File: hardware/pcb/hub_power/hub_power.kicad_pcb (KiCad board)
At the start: 2 copper layers, 74 x 86 mm, 58 parts, among them J1 XIAO, J10 BAT (JST-PH), J11 → 電源板, J12 → ハブ板, J13 USB-C, J2 OLED, J3 AS5600, J4 SPK IN, J5 SPK OUT, J6 REED, J7 TOGGLE, J8 BTN2, K31 G6S-2F DC5, Q1 MMUN2133LT1G, Q31 SS8050, U1 TPS61090RSAR, U2 MCP73871-2CCI/ML, U3 INA226AIDGSR

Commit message: Extended を 12 → 9 種類に減らす（$36.84 → $27.63）
🔒 2026-09-12 ユーザー「b でいいでしょ」。PowerBoost から写した定数のうち 3 つを Basic の値へ寄せた。
回路の意味はほとんど変えていない。

- R2 340kΩ（C17636・Extended）→ 330kΩ 0603 C23137（Basic）。
  LBO の閾値 0.5×(1+R1/R2) が 3.25V → 3.33V。80mV 早く知らせる側へ動く。
- R6 270kΩ（C17589・Extended）→ 220kΩ 0603 C22961、R7 100kΩ → 82kΩ 0603 C23254（どちらも Basic）。
  VPCC の分圧比 100/370=0.2703 → 82/302=0.2715 で差は 0.45%。
- C6 100µF 10V 1210（C23742・Extended・$0.45）→ 47µF 10V 1206 C96123（Basic・$0.27）を 2 個。
  Basic の 100µF は 6.3V 品しかなく、5.2V が掛かる所で耐圧を下げると残る容量が確実に減る
  （どれだけ減るかは曲線を見ていないので分からない）。耐圧 10V を保つため 2 個に分けた。
  ⚠ 足した C9 は PowerBoost に無い部品で、私が足したもの。

部品は表面実装 44 個・28 種類（Basic 19・Extended 9）。費用は約 $97 → 約 $88。

検査: check_sch 0 件・未配線 0・KiCad DRC のエラー 0（警告 99）・
      check_pcb は下限 0.15mm を割る組 0（いちばん近いのは 0.151mm）。
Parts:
- removed the R20 at (91.0, 114.0)
- removed the R5 at (90.9, 110.5)
- added LED1: RED, LED_SMD:LED_0805_2012Metric, F.Cu at (94.5, 114.0)
- added LED2: WHITE, LED_SMD:LED_0805_2012Metric, F.Cu at (94.3, 110.5)
- added Q1: MMUN2133LT1G, Package_TO_SOT_SMD:SOT-23, F.Cu at (87.0, 114.0)
- C6: value 100uF -> 47uF; footprint Capacitor_SMD:C_1210_3225Metric -> Capacitor_SMD:C_1206_3216Metric
- C9: renamed from R3; value 1.87M -> 47uF; footprint Resistor_SMD:R_0805_2012Metric -> Capacitor_SMD:C_1206_3216Metric
- R1: renamed from R2; value 340K -> 1.87M
- R13: renamed from Q1; value MMUN2133LT1G -> 200K; footprint Package_TO_SOT_SMD:SOT-23 -> Resistor_SMD:R_0805_2012Metric
- R2: renamed from R13; value 200K -> 330K
- R20: renamed from LED1; value RED -> 1K; footprint LED_SMD:LED_0805_2012Metric -> Resistor_SMD:R_0805_2012Metric
- R3: renamed from R4; value 200K -> 1.87M
- R4: renamed from R1; value 1.87M -> 200K
- R5: renamed from LED2; value WHITE -> 1K; footprint LED_SMD:LED_0805_2012Metric -> Resistor_SMD:R_0805_2012Metric
- R6: value 270K -> 220K
- R7: value 100K -> 82K
- moved R13 17.2 mm to (97.0, 100.0), turned to 90 degrees
- moved R2 14.0 mm to (87.4, 109.5), turned to 0 degrees
- moved R4 13.0 mm to (97.0, 111.0), turned to 90 degrees
- moved C9 8.38 mm to (103.1, 107.0)
- moved R3 4.52 mm to (94.9, 107.0)
- moved R20 3.50 mm to (91.0, 114.0)
- moved R1 3.40 mm to (84.0, 109.5)
- moved R5 3.40 mm to (90.9, 110.5)
- moved J12 0.69 mm to (100.1, 97.5)
- moved C6 0.36 mm to (97.0, 107.0)
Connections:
- C9 pad 2: FB -> GNDP
- R1 pad 1: LBI -> VSYS
- R1 pad 2: GNDP -> LBI
- R13 pad 1: LBO -> VSYS
- R13 pad 2: VSYS -> ENP
- R2 pad 1: VSYS -> LBI
- R2 pad 2: ENP -> GNDP
- R20 pad 1: GNDP -> N_Q1C
- R3 pad 1: FB -> V5P
- R3 pad 2: GNDP -> FB
- R4 pad 1: VSYS -> FB
- R4 pad 2: LBI -> GNDP
- R5 pad 1: GNDP -> V5P
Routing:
- net VLIPO: track 60.3 -> 44.0 mm
- net FB: track 19.4 -> 31.5 mm
- net VBUS: track 65.6 -> 77.0 mm
- net GNDP: track 180.3 -> 188.9 mm, vias 2 -> 3
- net VPCC: track 21.5 -> 29.0 mm
- net V5P: track 42.1 -> 48.6 mm
- net VSYS: track 70.7 -> 64.5 mm, vias 2 -> 3
- net THERM: track 17.3 -> 11.4 mm
- net PROG1: track 15.9 -> 20.4 mm
- net LBO: track 29.9 -> 25.6 mm
- net V33P: track 42.1 -> 37.9 mm
- net STAT2: track 26.6 -> 23.5 mm, vias 2 -> 0
- net ENP: track 23.6 -> 22.5 mm
- net STAT1: track 19.0 -> 19.6 mm
- net LBI: track 15.0 -> 14.4 mm

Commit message: J2（OLED）のピンの並びを逆にする — HS154L03W2C01 に合わせて
🔒 2026-09-12 ユーザー。OLED を 1.54" の HS154L03W2C01（SSD1309・I2C・C7465999・$6.94・在庫 1,242）
に替える前提で、J2 だけ並びを逆にした。穴の位置は動かしていない。

  いまの板の J2 : 1 SDA・2 SCL・3 3V3・4 GND
  パネル        : 1 GND・2 VCC・3 SCL・4 SDA（データシート 1.5 Pin Definition）
  逆にした結果  : 1 GND・2 V33・3 SCL・4 SDA

外形はデータシートの図より PCB 42.40 × 38.00 × 2.65、取付穴 φ3.0 × 4（中心間 37.40 × 33.00）、
端子はピッチ 2.54 のスルーホール 4 本。いまの OLED（70.1 × 48.1 × 8.5）より一回り小さく、
高さを決めていた 48.1 が 38 になる。

⚠ いまの OLED の線はこの板に挿せなくなる。戻すなら gen_sch.py の PORT_FLIP を空にする。
⚠ check_sch.py は PORT_FLIP を読んで同じ並びを期待するので、この 1 か所は機械で検算していない。

検査: check_sch 0 件・未配線 0・DRC エラー 0（警告 99）・check_pcb 0.151mm。
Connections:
- J2 pad 1: SDA -> GND
- J2 pad 2: SCL -> V33
- J2 pad 3: V33 -> SCL
- J2 pad 4: GND -> SDA
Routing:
- net GND: track 151.1 -> 158.8 mm
- net SDA: track 66.2 -> 69.4 mm
- net V33: track 68.5 -> 71.2 mm
- net SCL: track 69.8 -> 71.8 mm
- net BTN: track 48.2 -> 47.6 mm
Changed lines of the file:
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@@
 			(layers "*.Cu" "*.Mask")
 			(remove_unused_layers no)
-			(net 24 "SDA")
+			(net 10 "GND")
 		)
 		(pad "2" thru_hole circle
@@
 			(layers "*.Cu" "*.Mask")
 			(remove_unused_layers no)
-			(net 22 "SCL")
+			(net 35 "V33")
 		)
 		(pad "3" thru_hole circle
@@
 			(layers "*.Cu" "*.Mask")
 			(remove_unused_layers no)
-			(net 35 "V33")
+			(net 22 "SCL")
 		)
 		(pad "4" thru_hole circle
@@
 			(layers "*.Cu" "*.Mask")
 			(remove_unused_layers no)
-			(net 10 "GND")
+			(net 24 "SDA")
 		)
 		(model "${KICAD10_3DMODEL_DIR}/Connector_PinHeader_2.54mm.3dshapes/PinHeader_1x04_P2.54mm_Vertical.step"
@@
 	)
 	(segment
-		(start 81.7600 88.8600)
-		(end 81.7600 82.1492)
+		(start 66.5200 48.2200)
+		(end 67.6217 49.3217)
 		(width 0.200)
 		(layer "F.Cu")
@@
 	)
 	(segment
-		(start 81.7600 82.1492)
-		(end 69.3685 69.7577)
+		(start 67.6217 49.3217)
+		(end 67.6217 71.2352)
 		(width 0.200)
 		(layer "F.Cu")
@@
 	)
 	(segment
-		(start 69.3685 69.7577)
-		(end 68.7130 69.7577)
+		(start 67.6217 71.2352)
+		(end 68.8604 72.4739)
 		(width 0.200)
 		(layer "F.Cu")
@@
 	)
 	(segment
-		(start 68.7130 69.7577)
-		(end 65.4183 66.4630)
+		(start 68.8604 72.4739)
+		(end 69.9717 72.4739)
 		(width 0.200)
 		(layer "F.Cu")
@@
 	)
 	(segment
-		(start 65.4183 66.4630)
-		(end 65.4183 49.3217)
+		(start 69.9717 72.4739)
+		(end 81.7600 84.2622)
 		(width 0.200)
 		(layer "F.Cu")
@@
 	)
 	(segment
-		(start 65.4183 49.3217)
-		(end 66.5200 48.2200)
+		(start 81.7600 84.2622)
+		(end 81.7600 88.8600)
 		(width 0.200)
 		(layer "F.Cu")
@@
 	)
 	(segment
-		(start 69.0600 66.0000)
-		(end 66.5200 63.4600)
-		(width 0.200)
-		(layer "F.Cu")
-		(net 10)
-	)
-	(segment
-		(start 66.5200 63.4600)
-		(end 66.5200 50.7600)
-		(width 0.200)
-		(layer "F.Cu")
-		(net 10)
-	)
-	(segment
 		(start 66.5200 50.7600)
 		(end 67.6217 50.7600)
@@
 	)
 	(segment
+		(start 66.5200 50.7600)
+		(end 66.5200 71.0800)
+		(width 0.200)
+		(layer "F.Cu")
+		(net 10)
+	)
+	(segment
+		(start 66.5200 71.0800)
+		(end 69.0600 73.6200)
+		(width 0.200)
+		(layer "F.Cu")
+		(net 10)
+	)
+	(segment
 		(start 86.8400 43.1400)
 		(end 87.9417 44.2417)
@@
 	)
 	(segment
-		(start 69.0600 71.0800)
-		(end 79.2200 71.0800)
+		(start 86.8400 78.7000)
+		(end 85.7383 79.8017)
 		(width 0.200)
 		(layer "B.Cu")
@@
 	)
 	(segment
-		(start 79.2200 71.0800)
-		(end 86.8400 78.7000)
+		(start 85.7383 79.8017)
+		(end 80.3217 79.8017)
+		(width 0.200)
+		(layer "B.Cu")
+		(net 22)
+	)
+	(segment
+		(start 80.3217 79.8017)
+		(end 69.0600 68.5400)
 		(width 0.200)
 		(layer "B.Cu")
@@
 	)
 	(segment
-		(start 69.0600 73.6200)
-		(end 78.1183 73.6200)
+		(start 69.0600 66.0000)
+		(end 70.4983 66.0000)
 		(width 0.200)
 		(layer "B.Cu")
@@
 	)
 	(segment
-		(start 78.1183 73.6200)
+		(start 70.4983 66.0000)
 		(end 83.1983 78.7000)
 		(width 0.200)
@@
 	)
 	(segment
-		(start 69.0600 68.5400)
-		(end 79.2200 68.5400)
+		(start 69.0600 71.0800)
+		(end 78.1465 80.1665)
 		(width 0.200)
 		(layer "B.Cu")
@@
 	)
 	(segment
-		(start 79.2200 68.5400)
+		(start 78.1465 80.1665)
+		(end 87.9135 80.1665)
+		(width 0.200)
+		(layer "B.Cu")
+		(net 35)
+	)
+	(segment
+		(start 87.9135 80.1665)
 		(end 89.3800 78.7000)
 		(width 0.200)
@@
 	(segment
 		(start 89.3800 43.1400)
-		(end 89.3800 48.2200)
+		(end 89.3800 50.7600)
 		(width 0.200)
 		(layer "F.Cu")
@@
 	)
 	(segment
-		(start 89.3800 48.2200)
-		(end 69.0600 68.5400)
+		(start 89.3800 50.7600)
+		(end 69.0600 71.0800)
 		(width 0.200)
 		(layer "F.Cu")

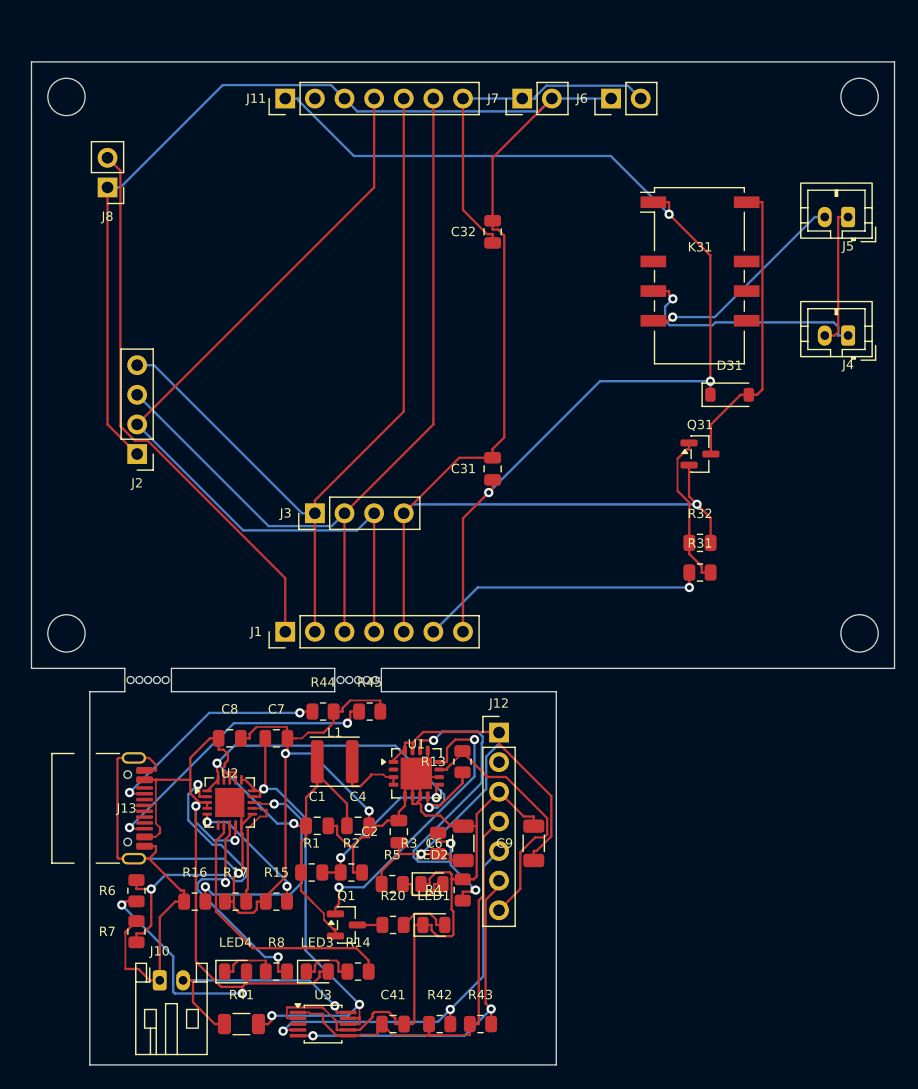
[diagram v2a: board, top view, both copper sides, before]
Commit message: 板を v6 の 1 枚（44 × 81.2）に起こし直して配線まで通す
外形・切り欠き・取付穴・部品の置き直し・自動配線まで一巡した。

- 外形 44 × 81.2 ＋ 上の縁の切り欠き（X 12〜22・Y 73 から上端）。パネルとミシン目は廃止
- 取付穴は M2 φ2.2 を 4 つ（X 3.5 と 40.5・Y 3.5 と 69.5）
- 座標系を「板の左下が原点・Y 上向き」に統一（bx()）。穴の名前から座標を引く仕組みは廃止
- 電源・充電・電流計は旧電源板の相対配置を 90 度回して電池の影（X 0〜35・Y 25〜75）へ。
  いちばん背が高いのがインダクタの 1.8 で、天井 4.4 に収まる
- 背の高い物は影の外。リレーは 90 度回して Y 12〜22.7、AS5600 は X 36.2・Y 7、
  リード・会話ボタン・電池は右の帯（X 35〜44）、スピーカーは左

🔴 CHECK_PADS（板の座標で「このパッドはここに来るはず」）を足した。XIAO のソケットを
最初 90 度で置いて、パッドが局所 +Y に並ぶ足形だったため 1 本目と 7 本目が X 方向に
並んでいたのを、これが捕まえた。鏡像事故はここで止める。

🔴 踏んだもの 2 つ:
- 取付穴（無メッキ）が部品の枠に入ると DRC が npth_inside_courtyard で落ちる。
  配線まで回してから気づいたので、置く段階で押し出すようにした
- リレーの駆動を電池の影（Y 70.5）に置いたら、リレーまで 53mm 離れて COL が
  1 本つながらなかった。リレーの隣へ移した

結果: 配線 633 本・貫通穴 49 個・**未配線 0**。
check_sch 0 件／check_pcb 下限 0.15mm に対していちばん近いのが 0.152mm／
KiCad DRC はエラー 0（警告は lib_footprint_issues とシルクの重なりだけ）。
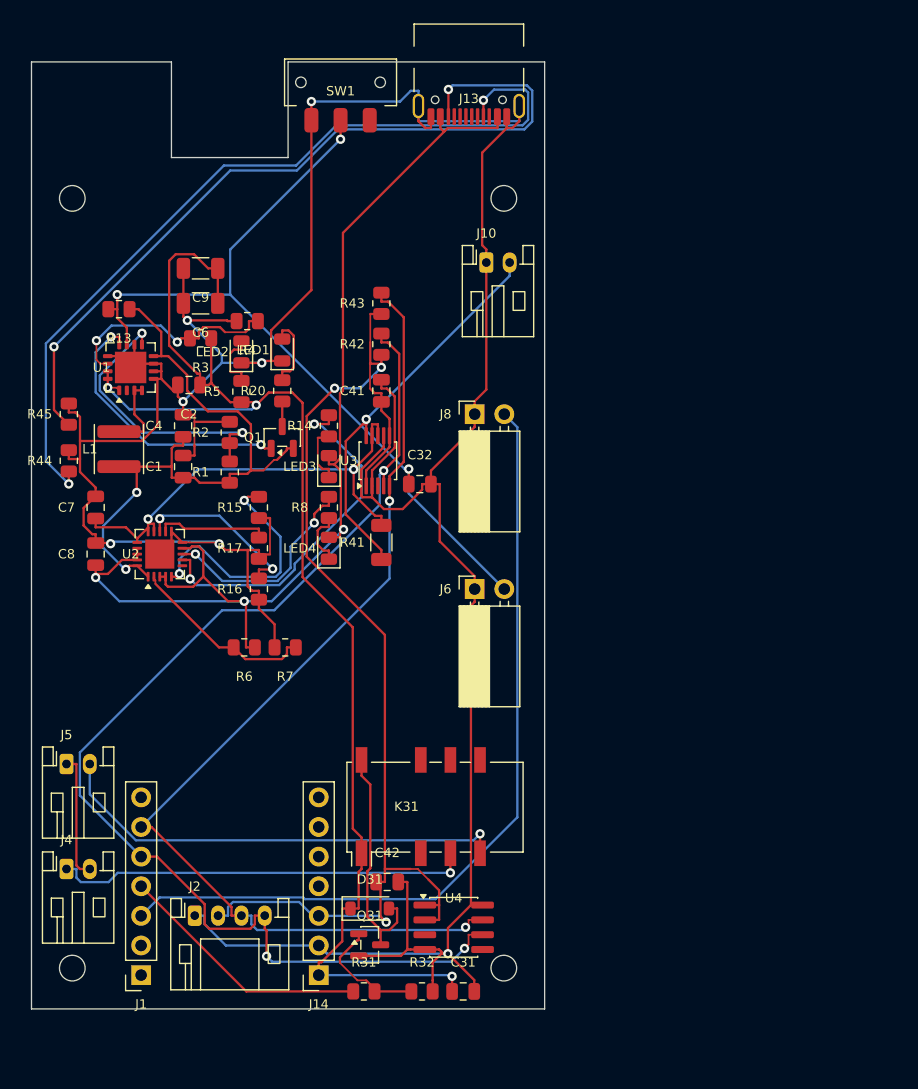
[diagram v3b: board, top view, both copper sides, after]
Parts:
- removed the ? at (63.0, 89.0)
- removed the ? at (63.0, 43.0)
- removed the ? at (131.0, 89.0)
- removed the ? at (131.0, 43.0)
- removed the C7 at (81.0, 98.0)
- removed J11: → 電源板, Connector_PinHeader_2.54mm:PinHeader_1x07_P2.54mm_Vertical
- removed J12: → ハブ板, Connector_PinHeader_2.54mm:PinHeader_1x07_P2.54mm_Vertical
- removed J3: AS5600, Connector_PinHeader_2.54mm:PinHeader_1x04_P2.54mm_Vertical
- removed J7: TOGGLE, Connector_PinHeader_2.54mm:PinHeader_1x02_P2.54mm_Vertical
- removed the R41 at (78.0, 122.5)
- removed the R44 at (85.0, 95.7)
- removed the U3 at (85.0, 122.5)
- added ?: , MountingHole:MountingHole_2.2mm_M2, F.Cu at (63.5, 117.7)
- added ?: , MountingHole:MountingHole_2.2mm_M2, F.Cu at (100.5, 117.7)
- added ?: , MountingHole:MountingHole_2.2mm_M2, F.Cu at (63.5, 51.7)
- added ?: , MountingHole:MountingHole_2.2mm_M2, F.Cu at (100.5, 51.7)
- added C42: 0.1uF, Capacitor_SMD:C_0805_2012Metric, F.Cu at (90.5, 110.3)
- added J14: XIAO PWR, Connector_PinSocket_2.54mm:PinSocket_1x07_P2.54mm_Vertical, F.Cu at (84.6, 118.3)
- added J4: SPK IN, Connector_JST:JST_PH_S2B-PH-K_1x02_P2.00mm_Horizontal, F.Cu at (63.0, 109.2)
- added J5: SPK OUT, Connector_JST:JST_PH_S2B-PH-K_1x02_P2.00mm_Horizontal, F.Cu at (63.0, 100.2)
- added R31: 1k, Resistor_SMD:R_0805_2012Metric, F.Cu at (88.5, 119.7)
- added R32: 10k, Resistor_SMD:R_0805_2012Metric, F.Cu at (93.5, 119.7)
- added SW1: MST-12D18G3, katanori:SW_Slide_MST-12D18G3, F.Cu at (86.5, 45.0)
- added U4: AS5600-ASOM, Package_SO:SOIC-8_3.9x4.9mm_P1.27mm, F.Cu at (96.2, 114.2)
- C7: renamed from J5; value SPK OUT -> 10uF; footprint Connector_JST:JST_PH_B2B-PH-K_1x02_P2.00mm_Vertical -> Capacitor_SMD:C_0805_2012Metric
- J1: value XIAO -> XIAO D0-D6; footprint Connector_PinHeader_2.54mm:PinHeader_1x07_P2.54mm_Vertical -> Connector_PinSocket_2.54mm:PinSocket_1x07_P2.54mm_Vertical
- J2: footprint Connector_PinHeader_2.54mm:PinHeader_1x04_P2.54mm_Vertical -> Connector_JST:JST_PH_S4B-PH-K_1x04_P2.00mm_Horizontal
- J6, J8: footprint Connector_PinHeader_2.54mm:PinHeader_1x02_P2.54mm_Vertical -> Connector_PinSocket_2.54mm:PinSocket_1x02_P2.54mm_Horizontal
- R41: renamed from R31; value 1k -> 10m; footprint Resistor_SMD:R_0805_2012Metric -> Resistor_SMD:R_1206_3216Metric
- R44: renamed from J4; value SPK IN -> 5.1k; footprint Connector_JST:JST_PH_B2B-PH-K_1x02_P2.00mm_Vertical -> Resistor_SMD:R_0805_2012Metric
- U3: renamed from R32; value 10k -> INA226AIDGSR; footprint Resistor_SMD:R_0805_2012Metric -> Package_SO:TSSOP-10_3x3mm_P0.5mm
- moved J13 70.9 mm to (97.5, 40.6), turned to 180 degrees
- moved C7 69.2 mm to (65.5, 78.2), turned to 90 degrees
- moved R44 67.7 mm to (63.2, 74.2), turned to 90 degrees
- moved J10 67.6 mm to (99.0, 57.2)
- moved R43 62.4 mm to (90.0, 60.7), turned to 90 degrees
- moved R42 58.5 mm to (90.0, 64.2), turned to 90 degrees
- moved C9 57.0 mm to (74.5, 57.7), turned to 180 degrees
- moved C41 54.3 mm to (90.0, 68.2), turned to 90 degrees
- moved D31 53.8 mm to (89.0, 112.6)
- moved R4 52.2 mm to (78.5, 62.2), turned to 180 degrees
- moved C6 51.5 mm to (74.5, 60.7), turned to 180 degrees
- moved LED1 51.0 mm to (81.5, 64.7), turned to 90 degrees
- moved K31 50.8 mm to (94.7, 103.8), turned to 90 degrees
- moved Q31 50.7 mm to (89.0, 115.7)
- moved R13 48.7 mm to (67.5, 61.2), turned to 180 degrees
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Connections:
- C1 pad 2: GNDP -> GND
- C2 pad 1: V5P -> V5
- C2 pad 2: GNDP -> GND
- C4 pad 2: GNDP -> GND
- C41 pad 1: V33P -> V33
- C41 pad 2: GNDP -> GND
- C6 pad 1: V5P -> V5
- C6 pad 2: GNDP -> GND
- C7 pad 1: SPKM -> VLIPO
- C7 pad 2: SPKO -> GND
- C8 pad 2: GNDP -> GND
- C9 pad 1: V5P -> V5
- C9 pad 2: GNDP -> GND
- J1 pad 1: BTN -> unconnected-(J1-Pin_1-Pad1)
- J1 pad 2: SDA -> unconnected-(J1-Pin_2-Pad2)
- J1 pad 3: SCL -> BTN
- J1 pad 4: V33 -> IN
- J1 pad 5: GND -> SDA
- J1 pad 6: IN -> SCL
- J1 pad 7: V5 -> unconnected-(J1-Pin_7-Pad7)
- J10 pad 1: GNDP -> GND
- J13 pad A1: GNDP -> GND
- J13 pad A12: GNDP -> GND
- J13 pad B1: GNDP -> GND
- J13 pad B12: GNDP -> GND
- J13 pad SH: GNDP -> GND
- LED1 pad 1: GNDP -> GND
- LED2 pad 1: GNDP -> GND
- R13 pad 2: ENP -> EN
- R15 pad 1: GNDP -> GND
- R16 pad 1: GNDP -> GND
- R17 pad 1: GNDP -> GND
- R2 pad 2: GNDP -> GND
- R3 pad 1: V5P -> V5
- R4 pad 2: GNDP -> GND
- R41 pad 1: IN -> BATP
- R41 pad 2: BASE -> VLIPO
- R42 pad 1: V33P -> V33
- R42 pad 2: SDAP -> SDA
- R43 pad 1: V33P -> V33
- R43 pad 2: SCLP -> SCL
- R44 pad 1: SPKP -> CC1
- R44 pad 2: SPKM -> GND
- R45 pad 2: GNDP -> GND
- R5 pad 1: V5P -> V5
- R7 pad 2: GNDP -> GND
- U1 pad 1: V5P -> V5
- U1 pad 10: GNDP -> GND
- U1 pad 11: ENP -> EN
- U1 pad 13: GNDP -> GND
- U1 pad 15: V5P -> V5
- U1 pad 16: V5P -> V5
- U1 pad 17: GNDP -> GND
- U1 pad 5: GNDP -> GND
- U1 pad 6: GNDP -> GND
- U1 pad 7: GNDP -> GND
- U2 pad 10: GNDP -> GND
- U2 pad 11: GNDP -> GND
- U2 pad 21: GNDP -> GND
- U3 pad 1: BASE -> V33
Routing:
- net GNDP: track 188.9 -> 0.00 mm, vias 3 -> 0
- net GND: track 158.8 -> 313.6 mm, vias 1 -> 7
- net CC1: track 19.9 -> 71.3 mm
- net V5P: track 48.6 -> 0.00 mm, vias 1 -> 0
- net CC2: track 25.6 -> 68.7 mm
- net EN: track 29.9 -> 70.4 mm, vias 0 -> 3
- net V33P: track 37.9 -> 0.00 mm
- net SDAP: track 33.0 -> 0.00 mm, vias 2 -> 0
- net SDA: track 69.4 -> 102.0 mm, vias 0 -> 3
- net SCLP: track 30.5 -> 0.00 mm, vias 2 -> 0
- net V33: track 71.2 -> 101.3 mm, vias 0 -> 3
- net BTN: track 47.6 -> 70.9 mm
- net V5: track 93.5 -> 116.6 mm
- net ENP: track 22.5 -> 0.00 mm
- net SPKO: track 18.4 -> 39.6 mm
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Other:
- board size 74 x 86 mm -> 44 x 81.2 mm

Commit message: リードと会話ボタンを 1 つの 4 ピン PH にまとめて、口 5 つを全部挿せるようにする
🔒 ユーザー 2026-09-13「別に線が二股になるのは構わないと思います」。

- 3 ピン（EN・BTN・GND）ではなく 4 ピンにした。GND を 2 本にすれば、1 つの端子へ線を
  2 本入れることも、線を割って継ぐこともせずに済む。並びは隣り合う 2 本ずつで分かれる
  ように 1 EN・2 GND →リード ／ 3 GND・4 BTN →会話ボタン
- 4 ピンの PH は幅 10.90 で、入るのは谷（幅 11.6）と上の縁（幅 12）の 2 か所だけ。
  OLED を上の縁、リード＋会話ボタンを谷にした
- スピーカーは箱の左なので、スピーカーへ出る J5 を左の帯に。ReSpeaker から来る J4 は右の帯へ

🔴 途中で J6 が 2 つできていた。PORT_REF から REED/BTN2 を外す編集が assert で止まって
書かれておらず、hub_ports 由来の J6（2 ピン）と新しい J6（4 ピン）が同じ ref で並び、
EN が GND に飲まれていた。check_sch が捕まえた。

結果: プラグの通り道 5 口すべて空き（J2 だけ通り道が電池の下で、挿し直すには電池を外す）。
配線 649 本・未配線 0・DRC エラー 0・check_sch 0 件・
check_pcb は下限 0.15mm に対していちばん近いのが 0.152mm。
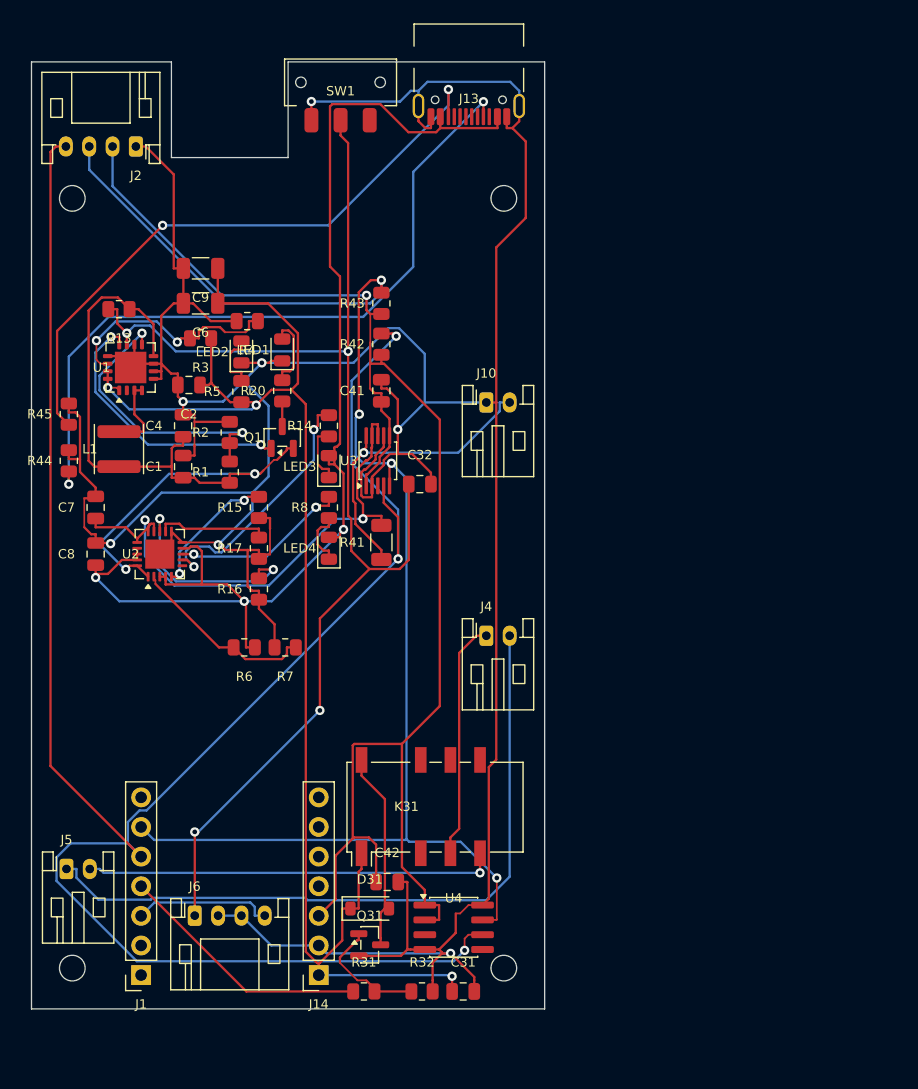
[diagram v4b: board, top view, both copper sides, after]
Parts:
- removed J8: BTN2, Connector_PinSocket_2.54mm:PinSocket_1x02_P2.54mm_Horizontal
- J4: renamed from J5; value SPK OUT -> SPK IN
- J5: renamed from J4; value SPK IN -> SPK OUT
- J6: value REED -> REED+BTN2; footprint Connector_PinSocket_2.54mm:PinSocket_1x02_P2.54mm_Horizontal -> Connector_JST:JST_PH_S4B-PH-K_1x04_P2.00mm_Horizontal
- moved J2 66.1 mm to (69.0, 47.2), turned to 180 degrees
- moved J4 37.6 mm to (99.0, 89.2)
- moved J6 36.9 mm to (74.0, 113.2), turned to 0 degrees
- moved J10 12.0 mm to (99.0, 69.2)
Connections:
- J4 pad 1: SPKM -> SPKP
- J4 pad 2: SPKO -> SPKM
- J5 pad 1: SPKP -> SPKM
- J5 pad 2: SPKM -> SPKO
- J6 pad 1: GND -> EN
- J6 pad 2: EN -> GND
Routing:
- net SDA: track 102.0 -> 181.1 mm
- net BTN: track 70.9 -> 12.0 mm
- net SPKM: track 10.8 -> 61.2 mm
- net EN: track 70.4 -> 110.1 mm, vias 3 -> 4
- net SCL: track 90.7 -> 126.1 mm, vias 2 -> 4
- net V33: track 101.3 -> 130.2 mm, vias 3 -> 1
- net GND: track 313.6 -> 339.6 mm
- net SPKP: track 35.8 -> 20.4 mm, vias 1 -> 0
- net CC2: track 68.7 -> 53.7 mm
- net VSYS: track 55.6 -> 67.8 mm
- net THERM: track 21.2 -> 11.4 mm
- net VBUS: track 97.4 -> 106.5 mm
- net CC1: track 71.3 -> 62.7 mm
- net STAT2: track 30.8 -> 22.4 mm
- net BATP: track 33.7 -> 26.8 mm
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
